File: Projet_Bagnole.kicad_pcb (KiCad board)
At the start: 2 copper layers, 50 parts, among them J1 USB_A, J2 Conn_01x03_Male, J3 Conn_01x04_Male, J4 AVR-ISP-6, M1 Motor_DC, M2 Stepper_Motor_bipolar, U1 ATmega16U2-AU, U2 DRV8210DRL, U3 MAX1811, Y1 Crystal_GND24

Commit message: V3
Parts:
- added ANT1: ANT3216LL00R2400A, Projet_Bagnole:ANT3216LL00R2400A, F.Cu at (277.7, 48.2)
- added C11: C, Capacitor_SMD:C_0603_1608Metric, F.Cu at (268.4, 58.7)
- added C12: C, Capacitor_SMD:C_0603_1608Metric, F.Cu at (283.4, 48.7)
- added C13: 10uF, Capacitor_SMD:C_0603_1608Metric, F.Cu at (272.4, 58.7)
- added C14: 10uF, Capacitor_SMD:C_0603_1608Metric, F.Cu at (280.8, 53.5)
- added L1: L, Inductor_SMD:L_0603_1608Metric, F.Cu at (287.4, 48.7)
- added R18: 4.7k, Resistor_SMD:R_0603_1608Metric, F.Cu at (276.4, 58.1)
- added R19: R, Resistor_SMD:R_0603_1608Metric, F.Cu at (280.8, 56.0)
- added U4: BM71BLE01FC2, Projet_Bagnole:BM71BLE01FC2, F.Cu at (267.4, 48.4)
- added U5: LM4040DBZ-2.5, Package_TO_SOT_SMD:SOT-23, F.Cu at (276.6, 54.5)
- M1: footprint Connector_PinHeader_2.54mm:PinHeader_1x02_P2.54mm_Vertical -> Projet_Bagnole:Motor_DC
- M2: footprint Connector_PinHeader_2.54mm:PinHeader_1x04_P2.54mm_Vertical -> Projet_Bagnole:Motor_Prop
- moved U3 203.5 mm to (259.8, 32.4)
- moved Y1 175.0 mm to (238.8, 31.0)
- moved J1 147.8 mm to (267.5, 74.1)
- moved C1 138.6 mm to (240.6, 51.2)
- moved C10 138.6 mm to (245.3, 48.6)
- moved C2 138.6 mm to (240.0, 58.8)
- moved C3 138.6 mm to (249.3, 48.5)
- moved C4 138.6 mm to (240.0, 56.2)
- moved C5 138.6 mm to (244.6, 51.1)
- moved C6 138.6 mm to (240.6, 53.7)
- moved C7 138.6 mm to (227.9, 58.3)
- moved C8 138.6 mm to (249.3, 46.0)
- moved C9 138.6 mm to (236.0, 56.2)
- moved D1 138.6 mm to (241.3, 43.5)
- moved D10 138.6 mm to (228.5, 53.2)
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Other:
- board outline added: 119 x 38 mm
- board text added: "Arrière"
- board text added: "Avant"
- board text added: "LA BAGNOLE DE DUHR DERYCKERE"

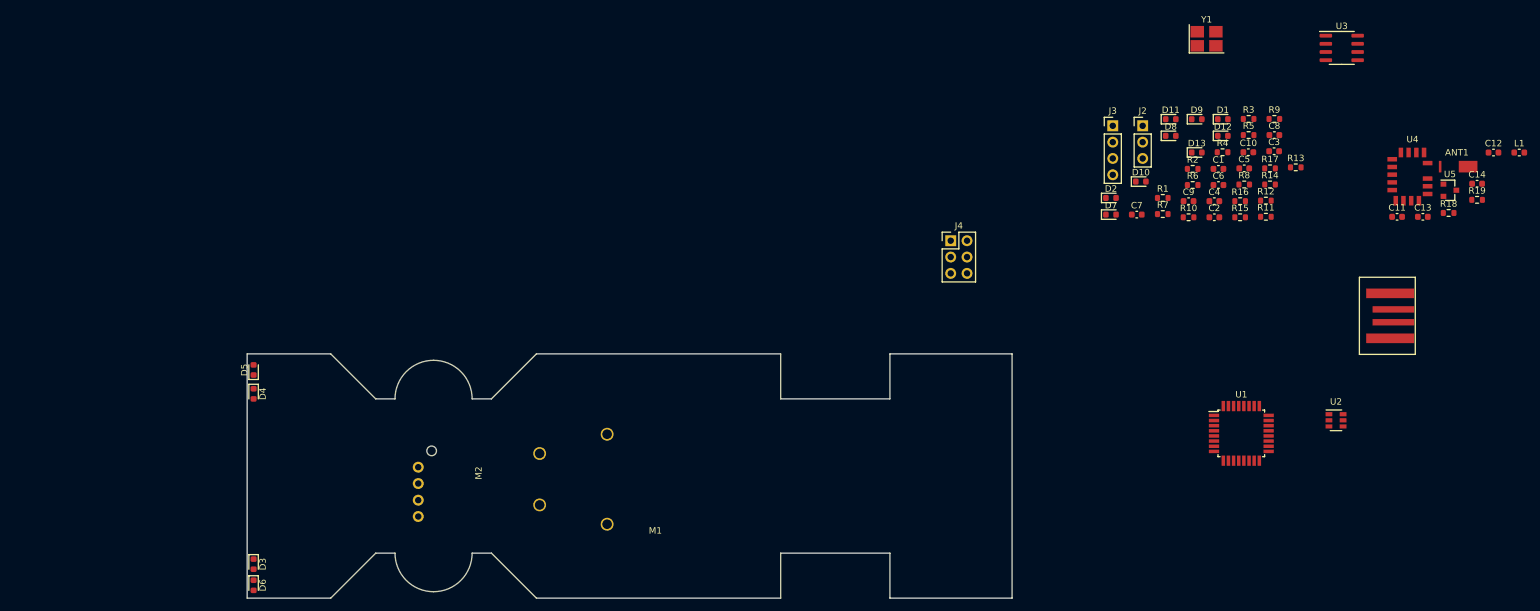
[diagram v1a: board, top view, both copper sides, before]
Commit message: 04/04 -Routage presque terminé
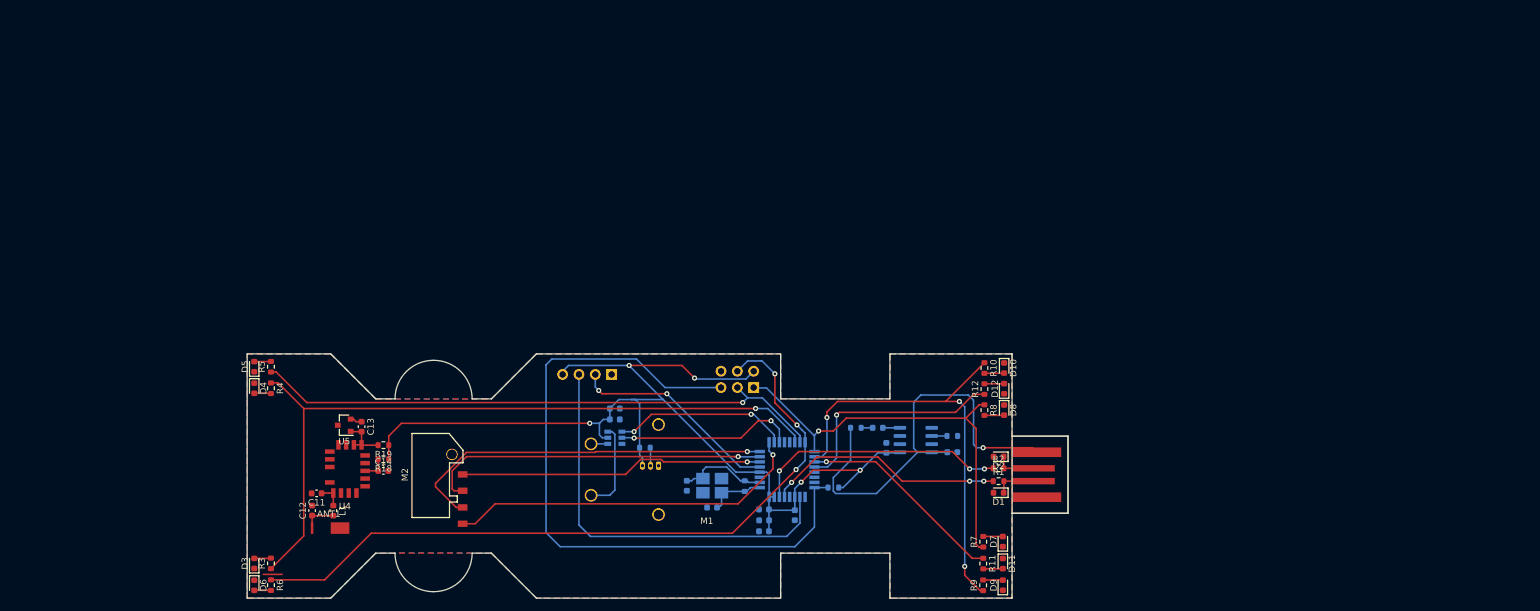
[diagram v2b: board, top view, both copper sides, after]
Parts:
- C1, C10, C2, C3, C4, C5, C6, C7, C8, C9, D13, J3, J4, R13, R14, R15, R16, R17, U1, U2, U3, Y1: moved to B.Cu
- J2: footprint Connector_PinHeader_2.54mm:PinHeader_1x03_P2.54mm_Vertical -> Connector_Molex:Molex_PicoBlade_53048-0310_1x03_P1.25mm_Horizontal; moved to B.Cu
- M2: footprint Projet_Bagnole:Motor_Prop -> rex-motors:micro-slider
- moved L1 192.7 mm to (102.9, 104.4), turned to 270 degrees
- moved C12 192.1 mm to (99.6, 104.4), turned to 90 degrees
- moved ANT1 184.3 mm to (102.2, 104.4)
- moved C14 175.9 mm to (110.7, 98.2)
- moved U5 175.9 mm to (104.6, 91.1), turned to 180 degrees
- moved R19 174.4 mm to (110.7, 94.2), turned to 180 degrees
- moved C11 173.5 mm to (100.3, 101.7), turned to 180 degrees
- moved R18 170.1 mm to (110.7, 96.4), turned to 180 degrees
- moved C13 168.3 mm to (107.3, 91.3), turned to 270 degrees
- moved U4 168.0 mm to (108.1, 101.9), turned to 180 degrees
- moved R3 167.1 mm to (93.2, 112.6), turned to 90 degrees
- moved R6 156.3 mm to (93.2, 116.0), turned to 270 degrees
- moved R5 156.3 mm to (93.2, 82.0), turned to 90 degrees
- moved R4 152.5 mm to (93.2, 85.3), turned to 270 degrees
- moved U2 112.2 mm to (146.7, 93.0), turned to 180 degrees
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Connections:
- ANT1 pad 1: (no net) -> Net-(ANT1-Pad1)
- C12 pad 1: Net-(ANT1-Pad~) -> Net-(ANT1-Pad1)
- L1 pad 2: Net-(ANT1-Pad~) -> Net-(ANT1-Pad1)
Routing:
- net VCC: track 0.00 -> 165.4 mm, vias 0 -> 5
- net LED3: track 0.00 -> 113.6 mm, vias 0 -> 3
- net LED1: track 0.00 -> 113.0 mm, vias 0 -> 1
- net RESET: track 0.00 -> 107.7 mm
- net LED2: track 0.00 -> 90.1 mm, vias 0 -> 1
- net LED5: track 0.00 -> 69.5 mm, vias 0 -> 3
- net VBUS: track 0.00 -> 67.0 mm, vias 0 -> 1
- net LED4: track 0.00 -> 65.3 mm, vias 0 -> 1
- net TX: track 0.00 -> 63.5 mm
- net M3: track 0.00 -> 58.6 mm, vias 0 -> 1
- net M4: track 0.00 -> 56.2 mm, vias 0 -> 1
- net M2: track 0.00 -> 53.4 mm, vias 0 -> 1
- net M1: track 0.00 -> 47.3 mm, vias 0 -> 1
- net D-: track 0.00 -> 39.7 mm, vias 0 -> 3
- net D+: track 0.00 -> 37.3 mm, vias 0 -> 3
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- added copper zone on B.Cu, net GND
- added copper zone on F.Cu, net GND
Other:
- board size 119 x 38 mm -> 127.7 x 38 mm

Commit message: Routage terminé (manque support roue)
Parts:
- J2, R16: moved to F.Cu
- moved R16 42.0 mm to (193.2, 98.5), turned to 180 degrees
- moved J2 38.2 mm to (191.5, 100.9), turned to 0 degrees
- moved C2 9.09 mm to (166.2, 99.3), turned to 270 degrees
- moved R13 3.04 mm to (165.6, 103.3)
- moved C4 2.00 mm to (159.8, 103.9)
- moved C5 2.00 mm to (155.9, 100.5)
- moved Y1 2.00 mm to (159.8, 100.5)
- moved M1 1.51 mm to (159.5, 105.2)
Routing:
- net GND: track 1.87 -> 540.1 mm
- net Net-(C5-Pad1): track 14.0 -> 20.0 mm
- net VBUS: track 67.0 -> 72.5 mm
- net Net-(C4-Pad1): track 9.05 -> 13.0 mm
- net TX: track 63.5 -> 66.6 mm
- net (no net): track 2.95 -> 0.00 mm, vias 0 -> 2
- net LED5: track 69.5 -> 72.4 mm
- net VCC: track 165.4 -> 162.7 mm, vias 5 -> 6
- net PWM1: track 27.3 -> 25.4 mm
- net PWM2: track 28.2 -> 26.5 mm
- net RESET: track 107.7 -> 106.1 mm
- net Net-(M1-Pad2): track 2.60 -> 4.16 mm
- net Net-(M1-Pad1): track 14.0 -> 15.6 mm
- net LED2: track 90.1 -> 91.1 mm
- net M3: track 58.6 -> 57.9 mm
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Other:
- board text added: "Vroum vroum"

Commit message: Fin des LEDs
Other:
- board text removed: "Vroum vroum"
